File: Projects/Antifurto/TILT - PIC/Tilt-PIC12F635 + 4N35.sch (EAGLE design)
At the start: 16 parts

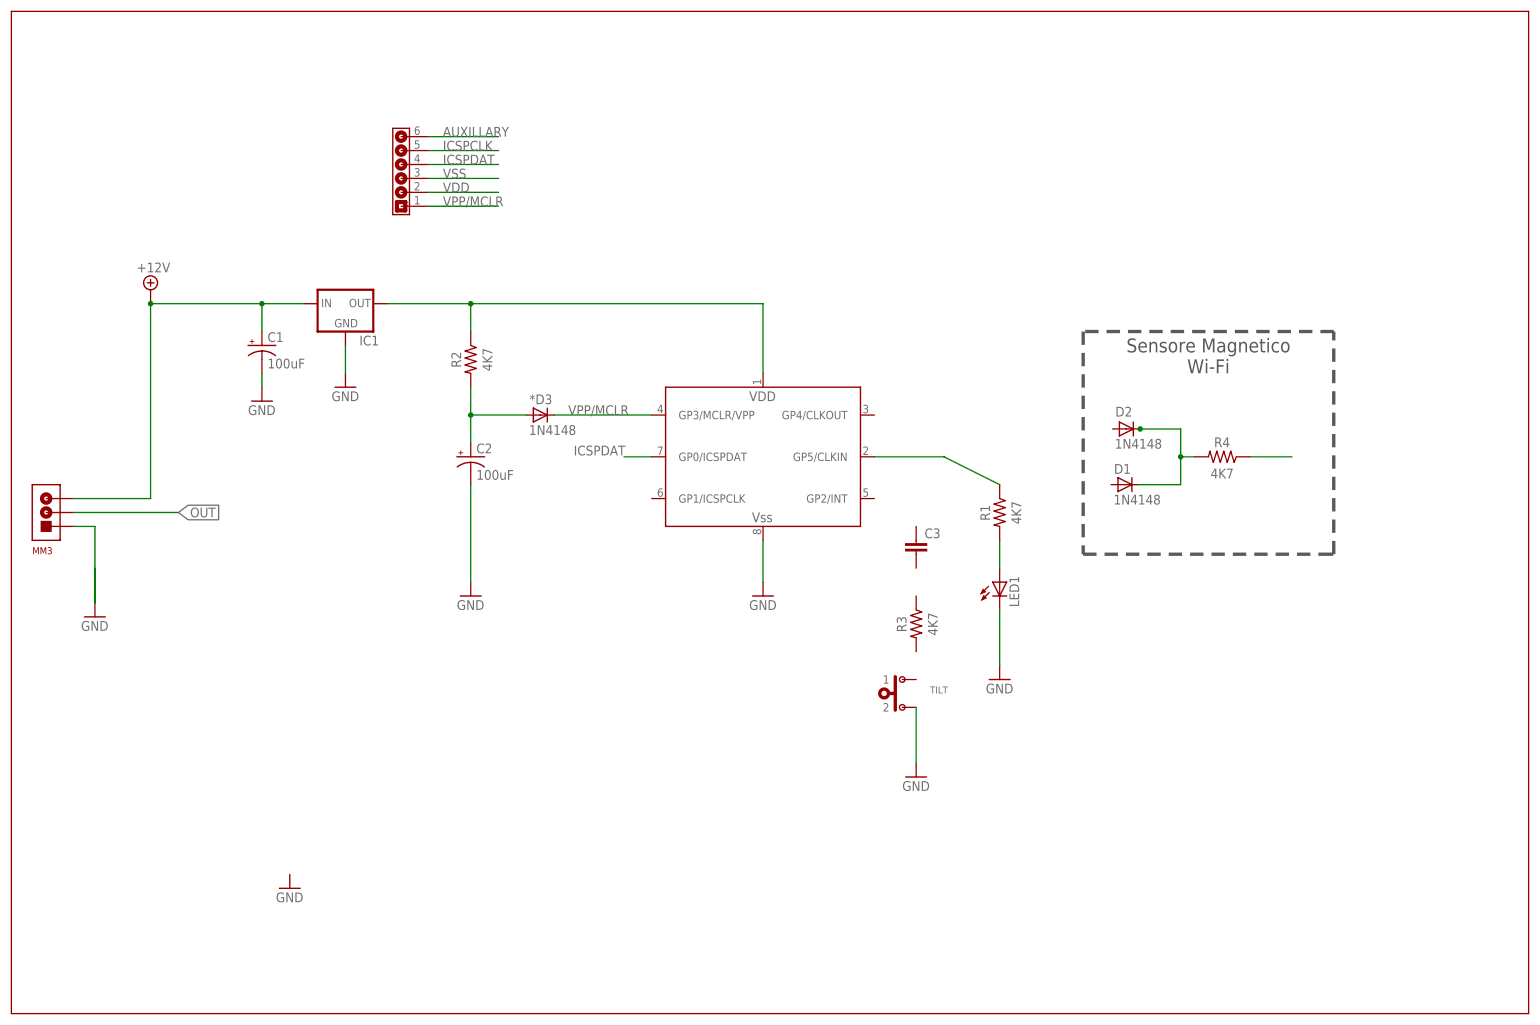
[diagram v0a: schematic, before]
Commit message: aggiornameti PIC12F635 + 4N35.sch
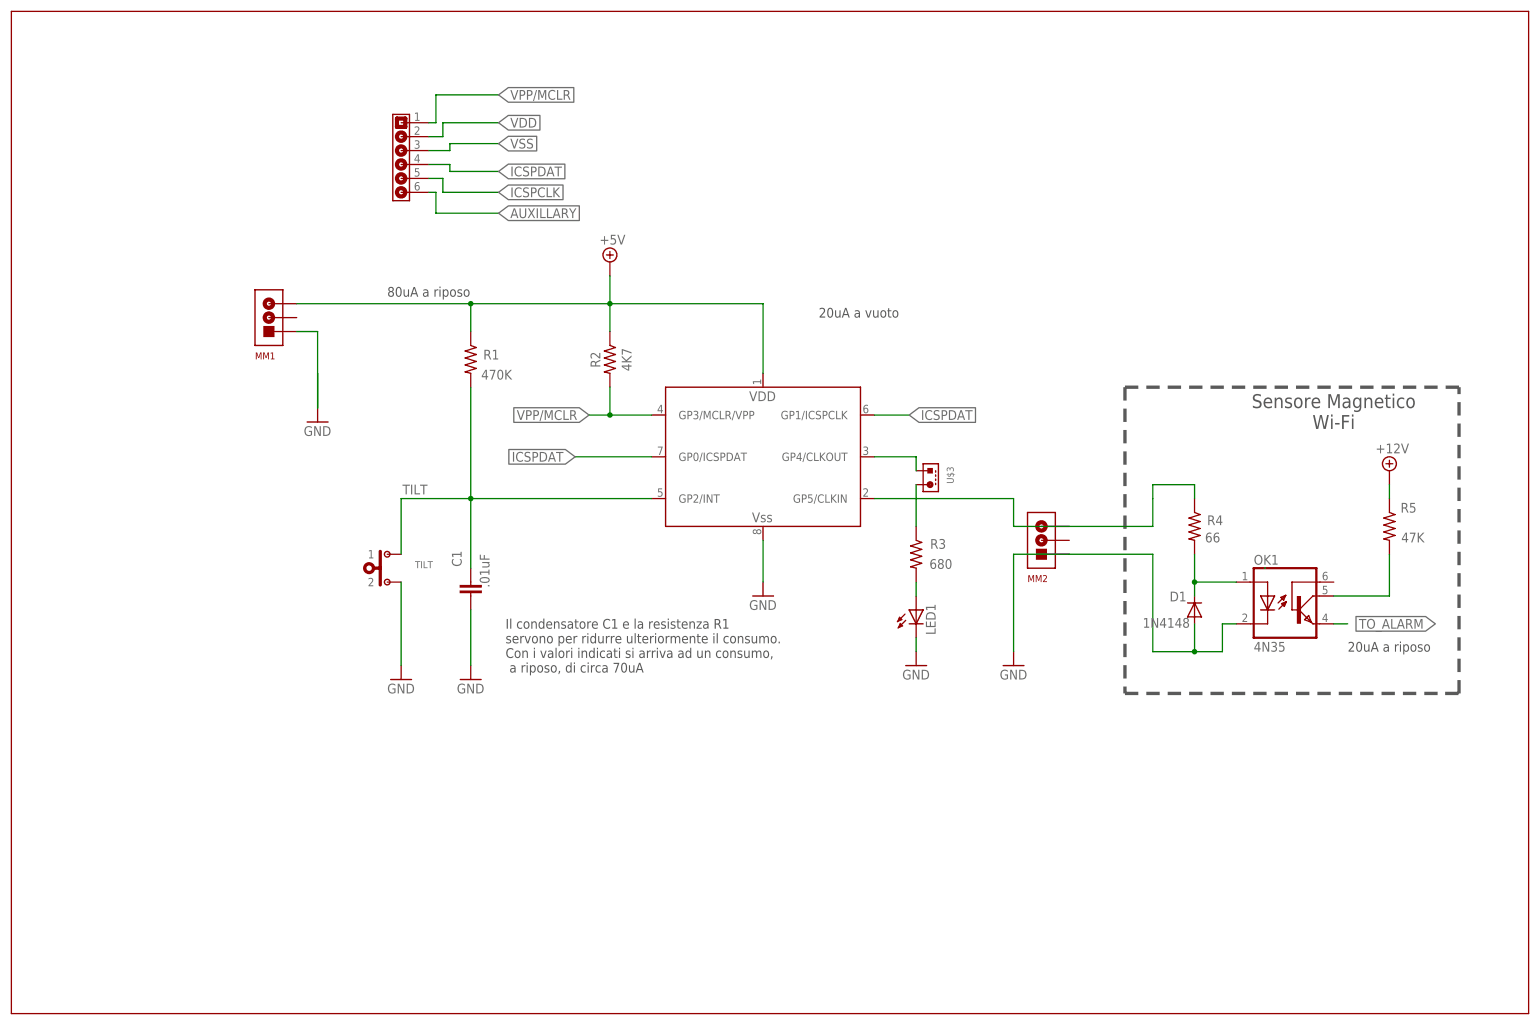
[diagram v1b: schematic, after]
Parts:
- removed *D3, D2: 1N4148, diode:1N4148DO35-10
- removed C2: 100uF, Ln-RCL:CPOL-US085CS-1AR
- removed C3: (no value), Ln-RCL:C-EU025-024X044
- removed IC1: (no value), Ln-v-reg:78LXX
- removed MM3: MAMMUTH03, Ln-Varie:MAMMUTH03
- added MM1, MM2: MAMMUTH03, Ln-Varie:MAMMUTH03
- added OK1: 4N35, Ln-TransDiodi:4N35
- added R5: 47K, rcl:R-US_0207/12
- added U$2: PIC12F635, LN-microchip:PIC12F635
- C1: value 100uF -> .01uF; device Ln-RCL:CPOL-US085CS-1AR -> Ln-RCL:C-EU025-024X044
- R1: value 4K7 -> 470K
- R3: value 4K7 -> 680
- R4: value 4K7 -> 66
- U$1: value PIC12F635 -> SIP06; device LN-microchip:PIC12F635 -> Ln-Varie:SIP06
- U$3: value SIP06 -> JUMPER2X1; device Ln-Varie:SIP06 -> Ln-Varie:JUMPER2X1
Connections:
- removed net OUT: MM3.2
- removed net SENSORE: R4.1
- new net +5V: R1.1, R2.1, U$2.VDD
- new net N$7: D1.C, OK1.A, R4.2
- new net N$8: OK1.COL, R5.2
- new net TILT: R1.2, TILT.1, U$2.GP2/INT
- new net TO_ALARM: OK1.EMI
- net +12V: now also R5.1; no longer C1.+, IC1.IN, MM3.3
- net AUXILLARY: now also U$1.P$6; no longer U$3.P$6
- net GND: now also C1.1, D1.A, MM2.1, OK1.C, TILT.2; no longer C2.-
- net ICSPCLK: now also U$1.P$5; no longer U$3.P$5
- net ICSPDAT: now also U$1.P$4, U$2.GP1/ICSPCLK; no longer U$3.P$4
- net N$2: now also R3.2; no longer R1.2
- net N$3: now also MM2.3, R4.1, U$2.GP5/CLKIN; no longer R1.1, U$1.GP5/CLKIN
- net N$5: now also U$2.GP4/CLKOUT, U$3.1; no longer *D3.A, C2.+, R2.2
- net N$6: now also R3.1, U$3.2; no longer D1.C, D2.C, R4.2
- net VDD: now also U$1.P$2; no longer IC1.OUT, R2.1, U$1.VDD, U$3.P$2
- net VPP/MCLR: now also R2.2, U$1.P$1, U$2.GP3/MCLR/VPP; no longer *D3.C, U$1.GP3/MCLR/VPP, U$3.P$1
- net VSS: now also MM1.1, U$1.P$3, U$2.VSS; no longer C1.-, IC1.GND, MM3.1, TILT.2, U$1.VSS, U$3.P$3
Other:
- note added: "20uA a riposo"
- note added: "20uA a vuoto"
- note added: "80uA a riposo"
- note added: "Il condensatore C1 e la resistenza R1 servono per ridurre ulteriormente il consumo. Con i valori indicati si arriva ad un consumo, a riposo, di circa 70uA"
- moved on the sheet: D1, LED1, R1, R2, R3, R4, TILT

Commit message: 2015-02-06 07:54 - commit with no comment
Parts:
- removed MM1, MM2: MAMMUTH03, Ln-Varie:MAMMUTH03
- removed U$3: JUMPER2X1, Ln-Varie:JUMPER2X1
- added *OCT, PWR: MAMMUTH03, Ln-Varie:MAMMUTH03
- added ALRM, JLED: JUMPER2X1, Ln-Varie:JUMPER2X1
- renumbered U$2 to UP1
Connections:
- removed net N$5: U$3.1, UP1.GP4/CLKOUT
- new net N$4: C1.2, UP1.GP2/INT
- net +12V: now also ALRM.1
- net +5V: now also PWR.3
- net GND: now also PWR.1; no longer C1.1, MM2.1
- net ICSPDAT: now also JLED.1
- net N$3: no longer MM2.3
- net N$6: now also JLED.2; no longer U$3.2
- net TILT: now also C1.1; no longer UP1.GP2/INT
- net TO_ALARM: now also ALRM.2
- net VSS: no longer MM1.1
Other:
- note added: "*OCT serve nel caso dovessi mettere l'accoppiatore ottico lontano dal uP."
- moved on the sheet: C1, LED1, R3, R5, TILT
